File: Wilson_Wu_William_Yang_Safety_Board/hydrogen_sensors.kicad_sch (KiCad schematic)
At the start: 13 parts, among them J5 Molex Micro-Fit 4 Pin, J9 Molex Micro-Fit 4 Pin, U15 INA826AID, U9 100 ohm

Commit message: sch update
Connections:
- net +3V0: no longer C6.2, U15.8 (VS+)
- net GND: now also U15.6 (REF)
- new net +3V3: C6.2, U15.8 (VS+)
- no-connect marks 2 -> 1
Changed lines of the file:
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@@
-	)
-	(no_connect
-		(at 101.6 80.01)
 	)
 	(no_connect
@@
 		(pts
 			(xy 40.64 74.93) (xy 40.64 77.47)
+		)
+		(stroke
+			(width 0)
+			(type default)
+		)
+	)
+	(wire
+		(pts
+			(xy 101.6 80.01) (xy 104.14 80.01)
 		)
 		(stroke
@@
 			)
 		)
-		(property "Value" "+3V0"
+		(property "Value" "+3V3"
 			(at 109.22 74.9299 90)
 			(effects
@@
 			)
 		)
-		(property "Datasheet" "https://www.vishay.com/docs/50020/rssd.pdf"
+		(property "Datasheet" "https://www.bourns.com/docs/Product-Datasheets/TC33.pdf"
 			(at 86.36 41.91 0)
 			(effects
@@
 					(size 1.27 1.27)
 				)
+				(hide yes)
 			)
 		)
@@
 					(unit 1)
 				)
+			)
+		)
+	)
+	(symbol
+		(lib_id "power:GND")
+		(at 104.14 80.01 90)
+		(unit 1)
+		(exclude_from_sim no)
+		(in_bom yes)
+		(on_board yes)
+		(dnp no)
+		(fields_autoplaced yes)
+		(property "Reference" "#PWR042"
+			(at 110.49 80.01 0)
+			(effects
+				(font
+					(size 1.27 1.27)
+				)
+				(hide yes)
+			)
+		)
+		(property "Value" "GND"
+			(at 107.95 80.0099 90)
+			(effects
+				(font
+					(size 1.27 1.27)
+				)
+				(justify right)
+			)
+		)
+		(property "Footprint" ""
+			(at 104.14 80.01 0)
+			(effects
+				(font
+					(size 1.27 1.27)
+				)
+				(hide yes)
+			)
+		)
+		(property "Datasheet" ""
+			(at 104.14 80.01 0)
+			(effects
+				(font
+					(size 1.27 1.27)
+				)
+				(hide yes)
+			)
+		)
+		(property "Description" "Power symbol creates a global label with name \"GND\" , ground"
+			(at 104.14 80.01 0)
+			(effects
+				(font
+					(size 1.27 1.27)
+				)
+				(hide yes)
+			)
+		)
+		(pin "1"
+		)
+		(instances
+			(project "Wilson_Wu_William_Yang_Safety_Board"
+				(path "/fa857c32-0741-4b91-b122-1a57686bb514/a02d46db-e0b8-42dd-a666-3d9580ac435e"
+					(reference "#PWR042")
+					(unit 1)
+				)

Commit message: schematic done
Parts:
- removed C13: 0.1uF, Capacitor_SMD:C_0805_2012Metric, symbol Device:C
- removed J5: Molex Micro-Fit 4 Pin, SMV_Connectors:4_pin0430450401, symbol SMV_Custom:Molex Micro-Fit 4 Pin
- added C14: 0.1uF, Capacitor_SMD:C_0805_2012Metric, symbol Device:C
- added J2: 22035035, SMV_Connectors:3pin_CON_22035035_MOL, symbol SMV_Custom:3-pin Mini Molex Spox
- added TP28, TP29, TP30, TP31: TestPoint, TestPoint:TestPoint_Pad_D1.0mm, symbol Connector:TestPoint
- C6: footprint (none) -> Capacitor_SMD:C_0805_2012Metric
- TP16, TP3: footprint TestPoint:TestPoint_Loop_D2.54mm_Drill1.5mm_Beaded -> TestPoint:TestPoint_Pad_D1.0mm
- U15: footprint D8 -> ina:D8-M
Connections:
- net +5V: now also C14.1, J2.1
- net GND: now also C14.2, J2.3
- net h_out: now also TP28.1
- net h_ref: now also TP29.1
- net h_sensor_2: now also TP31.1
- net ina_output: now also TP30.1
- net at R18.2: now also J2.2
- no-connect marks 1 -> 0
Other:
- moved on the sheet: R17, R18

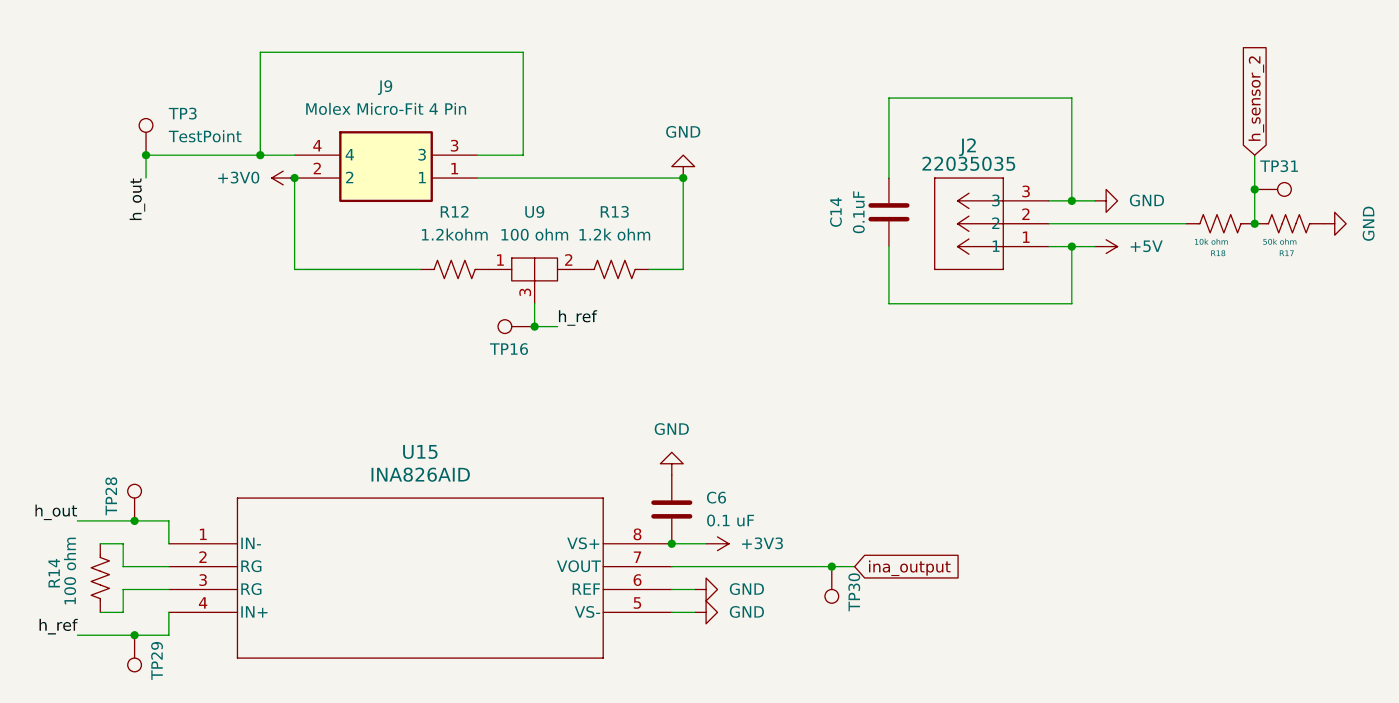
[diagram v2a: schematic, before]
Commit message: component placement
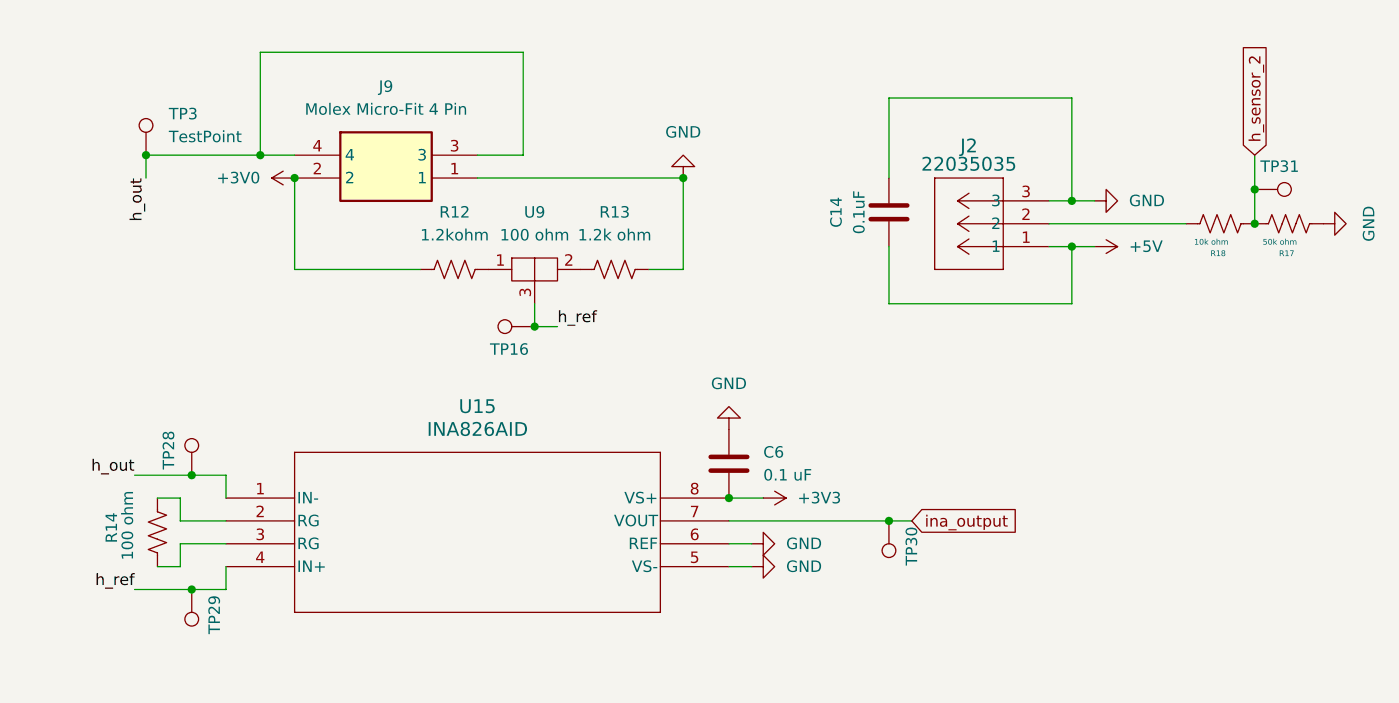
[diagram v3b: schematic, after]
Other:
- moved on the sheet: C6, R14, TP28, TP29, TP30, U15

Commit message: sch update
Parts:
- R14: value 100 ohm -> 500 ohm
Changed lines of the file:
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@@
 			)
 		)
-		(property "Value" "100 ohm"
+		(property "Value" "500 ohm"
 			(at 41.148 72.898 90)
 			(effects

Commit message: hydrogen
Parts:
- removed TP28, TP29: TestPoint, TestPoint:TestPoint_Pad_D1.0mm, symbol Connector:TestPoint
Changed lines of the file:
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@@
-	)
-	(junction
-		(at 48.26 67.31)
-		(diameter 0)
-		(color 0 0 0 0)
 	)
 	(junction
@@
 		(color 0 0 0 0)
 	)
-	(junction
-		(at 48.26 80.01)
-		(diameter 0)
-		(color 0 0 0 0)
-	)
 	(wire
 		(pts
@@
 	(wire
 		(pts
-			(xy 48.26 67.31) (xy 52.07 67.31)
-		)
-		(stroke
-			(width 0)
-			(type default)
-		)
-	)
-	(wire
-		(pts
 			(xy 146.05 41.91) (xy 146.05 48.26)
 		)
@@
 	(wire
 		(pts
-			(xy 41.91 80.01) (xy 48.26 80.01)
+			(xy 41.91 80.01) (xy 52.07 80.01)
 		)
 		(stroke
@@
 	(wire
 		(pts
-			(xy 41.91 67.31) (xy 48.26 67.31)
+			(xy 41.91 67.31) (xy 52.07 67.31)
 		)
 		(stroke
@@
 		(pts
 			(xy 43.18 31.75) (xy 55.88 31.75)
-		)
-		(stroke
-			(width 0)
-			(type default)
-		)
-	)
-	(wire
-		(pts
-			(xy 48.26 80.01) (xy 52.07 80.01)
 		)
 		(stroke
@@
 					(unit 1)
 				)
-			)
-		)
-	)
-	(symbol
-		(lib_id "Connector:TestPoint")
-		(at 48.26 80.01 180)
-		(unit 1)
-		(exclude_from_sim no)
-		(in_bom yes)
-		(on_board yes)
-		(dnp no)
-		(property "Reference" "TP29"
-			(at 50.8 82.804 90)
-			(effects
-				(font
-					(size 1.27 1.27)
-				)
-			)
-		)
-		(property "Value" "TestPoint"
-			(at 52.832 82.55 90)
-			(effects
-				(font
-					(size 1.27 1.27)
-				)
-				(hide yes)
-			)
-		)
-		(property "Footprint" "TestPoint:TestPoint_Pad_D1.0mm"
-			(at 43.18 80.01 0)
-			(effects
-				(font
-					(size 1.27 1.27)
-				)
-				(hide yes)
-			)
-		)
-		(property "Datasheet" "~"
-			(at 43.18 80.01 0)
-			(effects
-				(font
-					(size 1.27 1.27)
-				)
-				(hide yes)
-			)
-		)
-		(property "Description" "test point"
-			(at 48.26 80.01 0)
-			(effects
-				(font
-					(size 1.27 1.27)
-				)
-				(hide yes)
-			)
-		)
-		(pin "1"
-		)
-		(instances
-			(project "Wilson_Wu_William_Yang_Safety_Board"
-				(path "/fa857c32-0741-4b91-b122-1a57686bb514/a02d46db-e0b8-42dd-a666-3d9580ac435e"
-					(reference "TP29")
-					(unit 1)
-				)
-			)
-		)
-	)
-	(symbol
-		(lib_id "Connector:TestPoint")
-		(at 48.26 67.31 0)
-		(unit 1)
-		(exclude_from_sim no)
-		(in_bom yes)
-		(on_board yes)
-		(dnp no)
-		(property "Reference" "TP28"
-			(at 45.72 64.516 90)
-			(effects
-				(font
-					(size 1.27 1.27)
-				)
-			)
-		)
-		(property "Value" "TestPoint"
-			(at 43.688 64.77 90)
-			(effects
-				(font
-					(size 1.27 1.27)
-				)
-				(hide yes)
-			)
-		)
-		(property "Footprint" "TestPoint:TestPoint_Pad_D1.0mm"
-			(at 53.34 67.31 0)
-			(effects
-				(font
-					(size 1.27 1.27)
-				)
-				(hide yes)
-			)
-		)
-		(property "Datasheet" "~"
-			(at 53.34 67.31 0)
-			(effects
-				(font
-					(size 1.27 1.27)
-				)
-				(hide yes)
-			)
-		)
-		(property "Description" "test point"
-			(at 48.26 67.31 0)
-			(effects
-				(font
-					(size 1.27 1.27)
-				)
-				(hide yes)
-			)
-		)
-		(pin "1"
-		)
-		(instances
-			(project "Wilson_Wu_William_Yang_Safety_Board"
-				(path "/fa857c32-0741-4b91-b122-1a57686bb514/a02d46db-e0b8-42dd-a666-3d9580ac435e"
-					(reference "TP28")
-					(unit 1)
-				)

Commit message: Layout first draft
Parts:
- removed TP30: TestPoint, TestPoint:TestPoint_Pad_D1.0mm, symbol Connector:TestPoint
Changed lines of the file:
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@@
-	)
-	(junction
-		(at 125.73 72.39)
-		(diameter 0)
-		(color 0 0 0 0)
 	)
 	(junction
@@
 	(wire
 		(pts
-			(xy 125.73 72.39) (xy 128.27 72.39)
-		)
-		(stroke
-			(width 0)
-			(type default)
-		)
-	)
-	(wire
-		(pts
 			(xy 52.07 67.31) (xy 52.07 69.85)
 		)
@@
 	(wire
 		(pts
-			(xy 107.95 72.39) (xy 125.73 72.39)
+			(xy 107.95 72.39) (xy 128.27 72.39)
 		)
 		(stroke
@@
 					(unit 1)
 				)
-			)
-		)
-	)
-	(symbol
-		(lib_id "Connector:TestPoint")
-		(at 125.73 72.39 180)
-		(unit 1)
-		(exclude_from_sim no)
-		(in_bom yes)
-		(on_board yes)
-		(dnp no)
-		(property "Reference" "TP30"
-			(at 128.27 75.184 90)
-			(effects
-				(font
-					(size 1.27 1.27)
-				)
-			)
-		)
-		(property "Value" "TestPoint"
-			(at 130.302 74.93 90)
-			(effects
-				(font
-					(size 1.27 1.27)
-				)
-				(hide yes)
-			)
-		)
-		(property "Footprint" "TestPoint:TestPoint_Pad_D1.0mm"
-			(at 120.65 72.39 0)
-			(effects
-				(font
-					(size 1.27 1.27)
-				)
-				(hide yes)
-			)
-		)
-		(property "Datasheet" "~"
-			(at 120.65 72.39 0)
-			(effects
-				(font
-					(size 1.27 1.27)
-				)
-				(hide yes)
-			)
-		)
-		(property "Description" "test point"
-			(at 125.73 72.39 0)
-			(effects
-				(font
-					(size 1.27 1.27)
-				)
-				(hide yes)
-			)
-		)
-		(pin "1"
-		)
-		(instances
-			(project "Wilson_Wu_William_Yang_Safety_Board"
-				(path "/fa857c32-0741-4b91-b122-1a57686bb514/a02d46db-e0b8-42dd-a666-3d9580ac435e"
-					(reference "TP30")
-					(unit 1)
-				)

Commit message: layout
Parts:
- renumbered TP16 to h_ref_tp, TP3 to new_hsensor_output_tp1, TP31 to old_hsensor_tp1
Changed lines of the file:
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@@
 		(dnp no)
 		(fields_autoplaced yes)
-		(property "Reference" "TP3"
+		(property "Reference" "new_hsensor_output_tp1"
 			(at 45.72 27.1779 0)
 			(effects
@@
 			(project "Wilson_Wu_William_Yang_Safety_Board"
 				(path "/fa857c32-0741-4b91-b122-1a57686bb514/a02d46db-e0b8-42dd-a666-3d9580ac435e"
-					(reference "TP3")
+					(reference "new_hsensor_output_tp1")
 					(unit 1)
 				)
@@
 		(on_board yes)
 		(dnp no)
-		(property "Reference" "TP16"
+		(property "Reference" "h_ref_tp"
 			(at 83.566 53.34 90)
 			(effects
@@
 			(project "Wilson_Wu_William_Yang_Safety_Board"
 				(path "/fa857c32-0741-4b91-b122-1a57686bb514/a02d46db-e0b8-42dd-a666-3d9580ac435e"
-					(reference "TP16")
+					(reference "h_ref_tp")
 					(unit 1)
 				)
@@
 		(on_board yes)
 		(dnp no)
-		(property "Reference" "TP31"
+		(property "Reference" "old_hsensor_tp1"
 			(at 169.164 33.02 90)
 			(effects
@@
 			(project "Wilson_Wu_William_Yang_Safety_Board"
 				(path "/fa857c32-0741-4b91-b122-1a57686bb514/a02d46db-e0b8-42dd-a666-3d9580ac435e"
-					(reference "TP31")
-					(unit 1)
-				)
+					(reference "old_hsensor_tp1")
+					(unit 1)
+				)

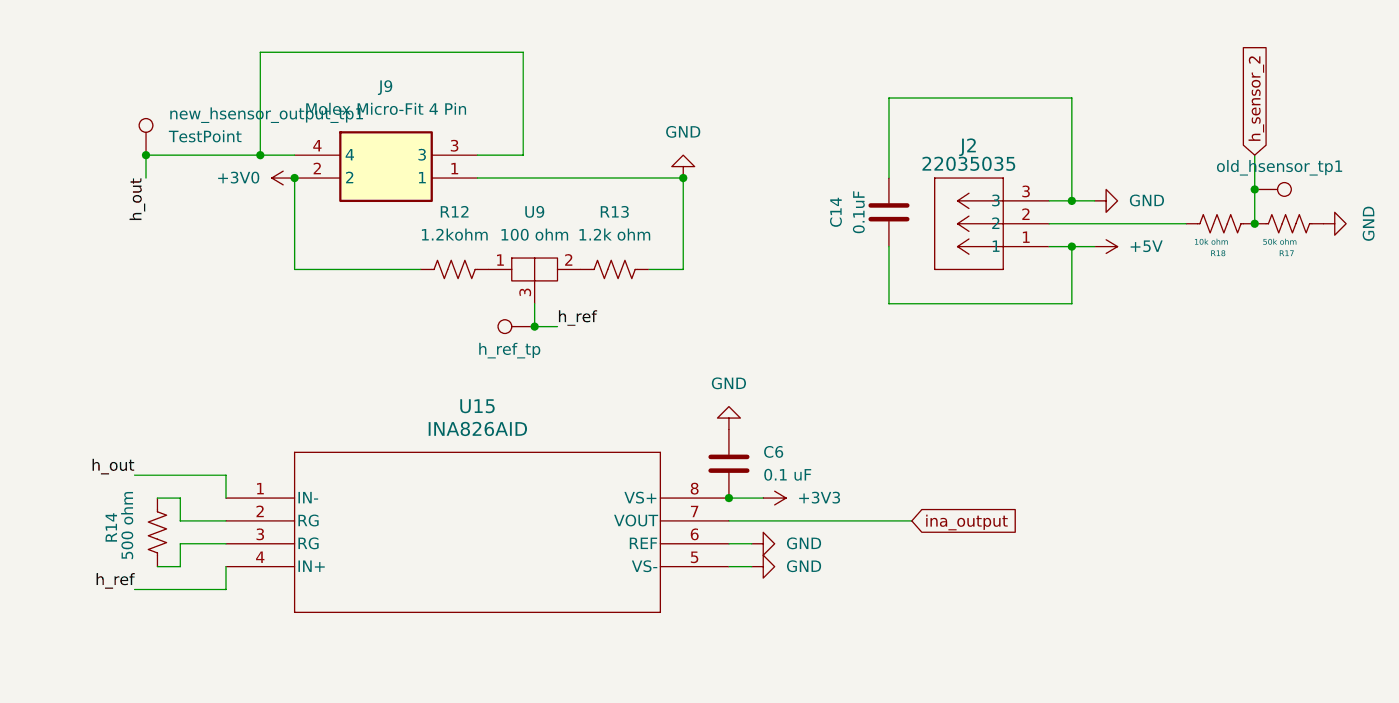
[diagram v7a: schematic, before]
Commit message: layout fixes
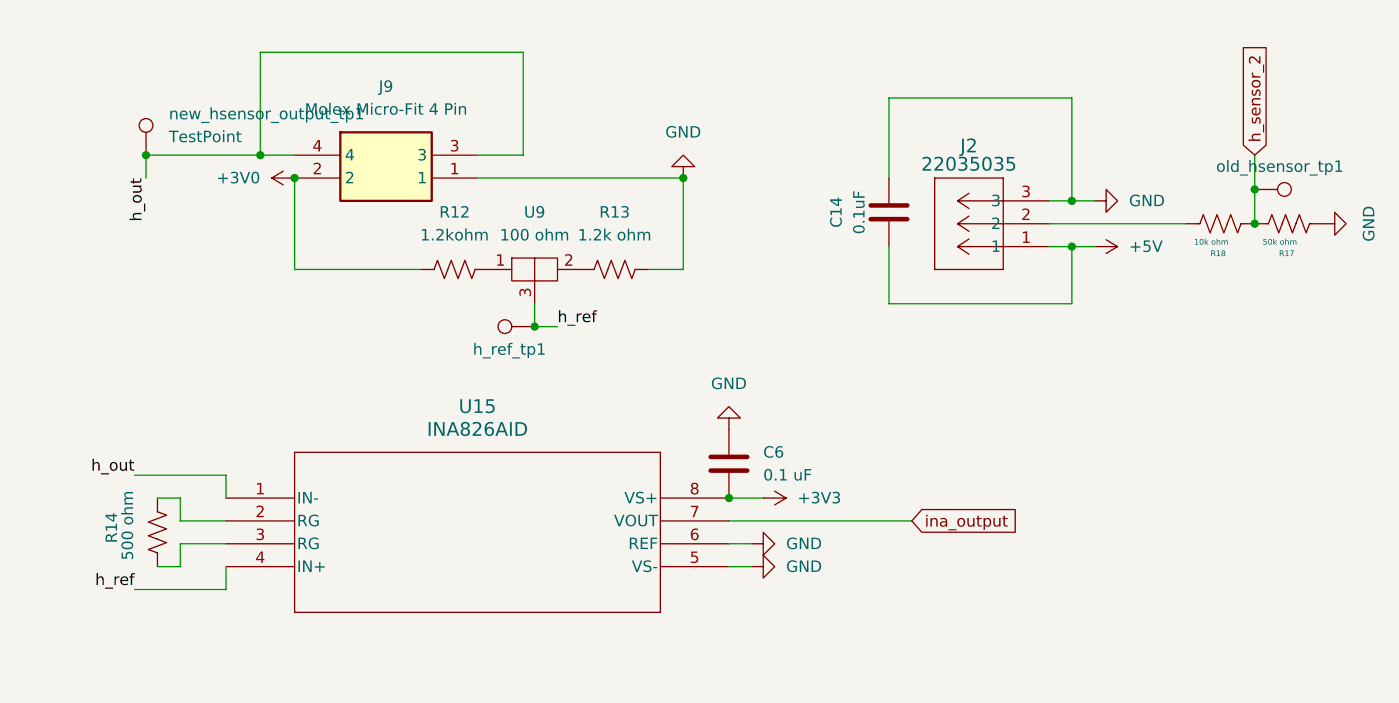
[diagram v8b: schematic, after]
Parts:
- renumbered h_ref_tp to h_ref_tp1
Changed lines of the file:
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@@
 		(on_board yes)
 		(dnp no)
-		(property "Reference" "h_ref_tp"
+		(property "Reference" "h_ref_tp1"
 			(at 83.566 53.34 90)
 			(effects
@@
 			(project "Wilson_Wu_William_Yang_Safety_Board"
 				(path "/fa857c32-0741-4b91-b122-1a57686bb514/a02d46db-e0b8-42dd-a666-3d9580ac435e"
-					(reference "h_ref_tp")
+					(reference "h_ref_tp1")
 					(unit 1)
 				)
